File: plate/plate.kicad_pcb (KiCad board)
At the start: 2 copper layers, 67.2 x 29.1 mm, 4 parts

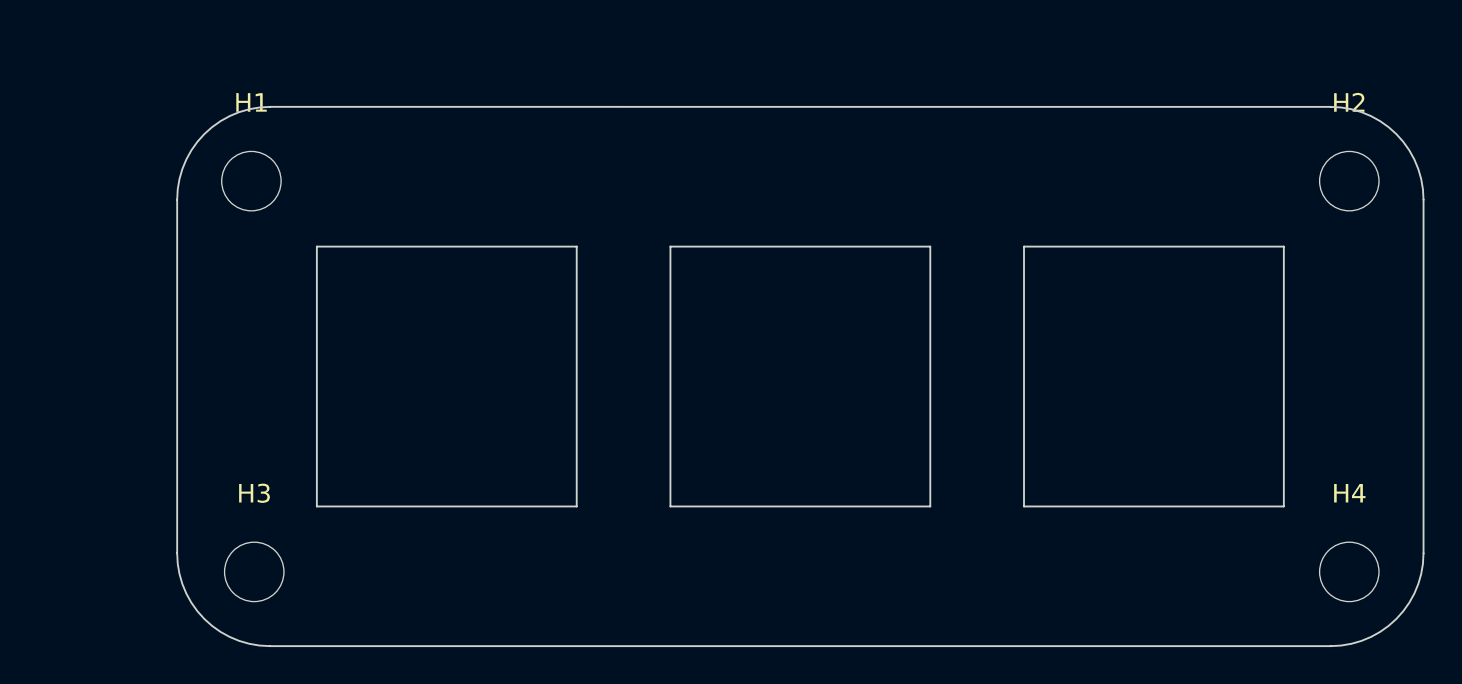
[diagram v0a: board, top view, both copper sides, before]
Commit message: Wire up extra microcontroller pins to a header, align mounting holes
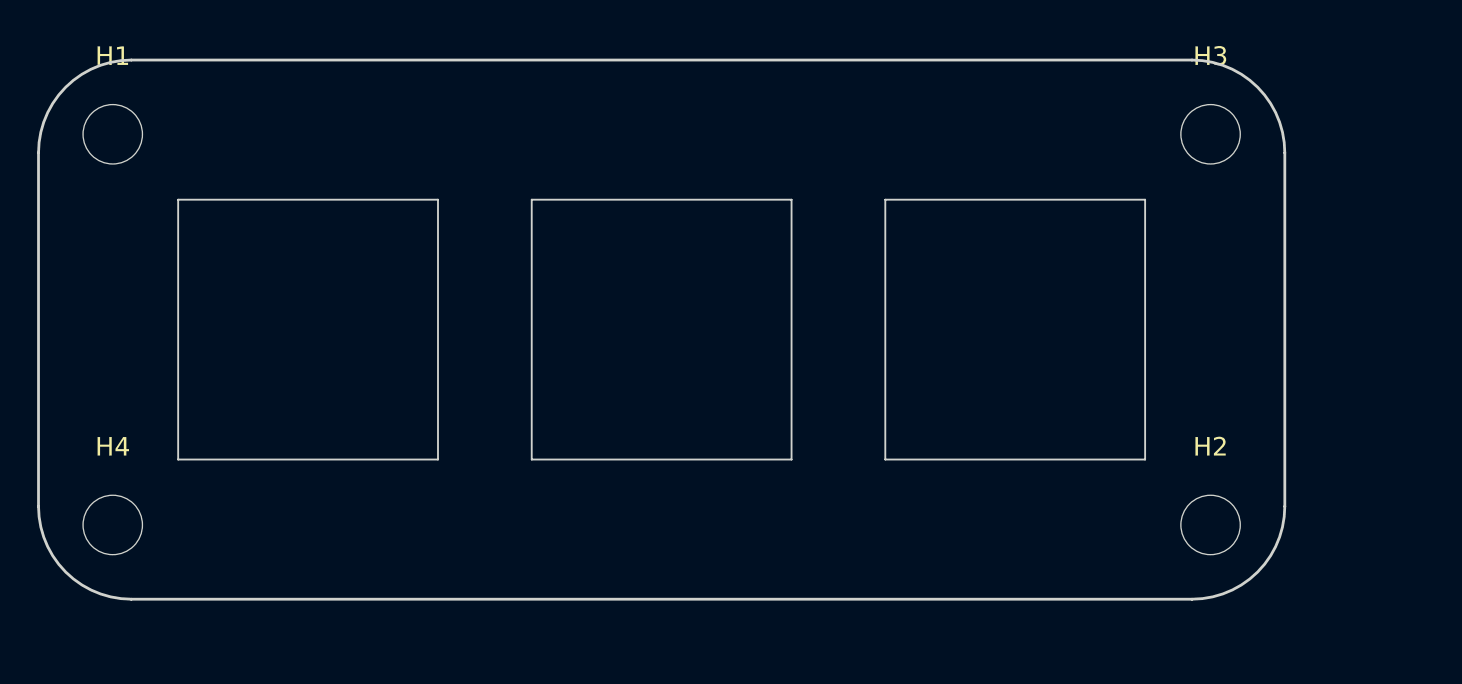
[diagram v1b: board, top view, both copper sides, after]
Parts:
- moved H4 66.7 mm to (114.0, 97.5)
- moved H3 56.7 mm to (173.2, 76.5)
- moved H2 20.0 mm to (173.2, 97.5)
- moved H1 7.89 mm to (114.0, 76.5)
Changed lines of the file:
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@@
     (pad_to_mask_clearance 0)
     (aux_axis_origin 117.496765 74.9968)
-    (grid_origin 122.496765 79.9968)
+    (grid_origin 172.1764 77.4722)
     (pcbplotparams
       (layerselection 0x00010fc_ffffffff)
@@
   (net 0 "")
   (footprint "MountingHole:MountingHole_3.2mm_M3" (layer "F.Cu")
-    (at 180.650815 78.9968)
+    (at 114.026185 97.522207)
+    (descr "Mounting Hole 3.2mm, no annular, M3")
+    (tags "mounting hole 3.2mm no annular m3")
+    (property "Sheetfile" "plate.kicad_sch")
+    (property "Sheetname" "")
+    (attr exclude_from_pos_files)
+    (fp_text reference "H4" (at 0 -4.2) (layer "F.SilkS")
+      (effects (font (size 1 1) (thickness 0.15)))
+    )
+    (fp_text value "MountingHole" (at 0 4.2) (layer "F.Fab")
+      (effects (font (size 1 1) (thickness 0.15)))
+    )
+    (fp_text user "${REFERENCE}" (at 0 0) (layer "F.Fab")
+      (effects (font (size 1 1) (thickness 0.15)))
+    )
+    (fp_circle (center 0 0) (end 3.2 0) (layer "Cmts.User") (width 0.15) (fill none))
+    (fp_circle (center 0 0) (end 3.45 0) (layer "F.CrtYd") (width 0.05) (fill none))
+    (pad "" np_thru_hole circle (at 0 0) (size 3.2 3.2) (drill 3.2) (layers *.Cu *.Mask))
+  )
+  (footprint "MountingHole:MountingHole_3.2mm_M3" (layer "F.Cu")
+    (at 114.0262 76.4722)
+    (descr "Mounting Hole 3.2mm, no annular, M3")
+    (tags "mounting hole 3.2mm no annular m3")
+    (property "Sheetfile" "plate.kicad_sch")
+    (property "Sheetname" "")
+    (attr exclude_from_pos_files)
+    (fp_text reference "H1" (at 0 -4.2) (layer "F.SilkS")
+      (effects (font (size 1 1) (thickness 0.15)))
+    )
+    (fp_text value "MountingHole" (at 0 4.2) (layer "F.Fab")
+      (effects (font (size 1 1) (thickness 0.15)))
+    )
+    (fp_text user "${REFERENCE}" (at 0 0) (layer "F.Fab")
+      (effects (font (size 1 1) (thickness 0.15)))
+    )
+    (fp_circle (center 0 0) (end 3.2 0) (layer "Cmts.User") (width 0.15) (fill none))
+    (fp_circle (center 0 0) (end 3.45 0) (layer "F.CrtYd") (width 0.05) (fill none))
+    (pad "" np_thru_hole circle (at 0 0) (size 3.2 3.2) (drill 3.2) (layers *.Cu *.Mask))
+  )
+  (footprint "MountingHole:MountingHole_3.2mm_M3" (layer "F.Cu")
+    (at 173.1764 97.522207)
     (descr "Mounting Hole 3.2mm, no annular, M3")
     (tags "mounting hole 3.2mm no annular m3")
@@
   )
   (footprint "MountingHole:MountingHole_3.2mm_M3" (layer "F.Cu")
-    (at 180.650815 100.05093)
-    (descr "Mounting Hole 3.2mm, no annular, M3")
-    (tags "mounting hole 3.2mm no annular m3")
-    (property "Sheetfile" "plate.kicad_sch")
-    (property "Sheetname" "")
-    (attr exclude_from_pos_files)
-    (fp_text reference "H4" (at 0 -4.2) (layer "F.SilkS")
-      (effects (font (size 1 1) (thickness 0.15)))
-    )
-    (fp_text value "MountingHole" (at 0 4.2) (layer "F.Fab")
-      (effects (font (size 1 1) (thickness 0.15)))
-    )
-    (fp_text user "${REFERENCE}" (at 0 0) (layer "F.Fab")
-      (effects (font (size 1 1) (thickness 0.15)))
-    )
-    (fp_circle (center 0 0) (end 3.2 0) (layer "Cmts.User") (width 0.15) (fill none))
-    (fp_circle (center 0 0) (end 3.45 0) (layer "F.CrtYd") (width 0.05) (fill none))
-    (pad "" np_thru_hole circle (at 0 0) (size 3.2 3.2) (drill 3.2) (layers *.Cu *.Mask))
-  )
-  (footprint "MountingHole:MountingHole_3.2mm_M3" (layer "F.Cu")
-    (at 121.650815 100.05093)
+    (at 173.1764 76.4722)
     (descr "Mounting Hole 3.2mm, no annular, M3")
     (tags "mounting hole 3.2mm no annular m3")
@@
     (pad "" np_thru_hole circle (at 0 0) (size 3.2 3.2) (drill 3.2) (layers *.Cu *.Mask))
   )
-  (footprint "MountingHole:MountingHole_3.2mm_M3" (layer "F.Cu")
-    (at 121.496765 78.9968)
-    (descr "Mounting Hole 3.2mm, no annular, M3")
-    (tags "mounting hole 3.2mm no annular m3")
-    (property "Sheetfile" "plate.kicad_sch")
-    (property "Sheetname" "")
-    (attr exclude_from_pos_files)
-    (fp_text reference "H1" (at 0 -4.2) (layer "F.SilkS")
-      (effects (font (size 1 1) (thickness 0.15)))
-    )
-    (fp_text value "MountingHole" (at 0 4.2) (layer "F.Fab")
-      (effects (font (size 1 1) (thickness 0.15)))
-    )
-    (fp_text user "${REFERENCE}" (at 0 0) (layer "F.Fab")
-      (effects (font (size 1 1) (thickness 0.15)))
-    )
-    (fp_circle (center 0 0) (end 3.2 0) (layer "Cmts.User") (width 0.15) (fill none))
-    (fp_circle (center 0 0) (end 3.45 0) (layer "F.CrtYd") (width 0.05) (fill none))
-    (pad "" np_thru_hole circle (at 0 0) (size 3.2 3.2) (drill 3.2) (layers *.Cu *.Mask))
-  )
-  (gr_line (start 158.074915 82.5241) (end 158.074915 96.525) (layer "Edge.Cuts") (width 0.1))
-  (gr_line (start 144.074115 96.525) (end 144.074115 82.5241) (layer "Edge.Cuts") (width 0.1))
-  (gr_line (start 179.650815 104.05093) (end 122.496765 104.05093) (layer "Edge.Cuts") (width 0.1))
-  (gr_line (start 144.074115 82.5241) (end 158.074915 82.5241) (layer "Edge.Cuts") (width 0.1))
-  (gr_line (start 125.024105 96.525) (end 125.024105 82.5241) (layer "Edge.Cuts") (width 0.1))
-  (gr_line (start 139.025015 96.525) (end 125.024105 96.525) (layer "Edge.Cuts") (width 0.1))
-  (gr_line (start 177.124915 96.525) (end 163.124215 96.525) (layer "Edge.Cuts") (width 0.1))
-  (gr_arc (start 117.496765 79.9968) (mid 118.961231 76.461266) (end 122.496765 74.9968) (layer "Edge.Cuts") (width 0.1))
-  (gr_line (start 184.650815 79.9968) (end 184.650815 99.05093) (layer "Edge.Cuts") (width 0.1))
-  (gr_line (start 122.496765 74.9936) (end 179.650815 74.9968) (layer "Edge.Cuts") (width 0.1))
-  (gr_arc (start 122.496765 104.05093) (mid 118.961231 102.586464) (end 117.496765 99.05093) (layer "Edge.Cuts") (width 0.1))
-  (gr_arc (start 179.650815 74.9968) (mid 183.186349 76.461266) (end 184.650815 79.9968) (layer "Edge.Cuts") (width 0.1))
-  (gr_line (start 117.496765 99.05093) (end 117.496765 79.9968) (layer "Edge.Cuts") (width 0.1))
-  (gr_line (start 177.124915 82.5241) (end 177.124915 96.525) (layer "Edge.Cuts") (width 0.1))
-  (gr_line (start 163.124215 96.525) (end 163.124215 82.5241) (layer "Edge.Cuts") (width 0.1))
-  (gr_line (start 163.124215 82.5241) (end 177.124915 82.5241) (layer "Edge.Cuts") (width 0.1))
-  (gr_line (start 158.074915 96.525) (end 144.074115 96.525) (layer "Edge.Cuts") (width 0.1))
-  (gr_arc (start 184.650815 99.05093) (mid 183.186349 102.586464) (end 179.650815 104.05093) (layer "Edge.Cuts") (width 0.1))
-  (gr_line (start 125.024105 82.5241) (end 139.025015 82.5241) (layer "Edge.Cuts") (width 0.1))
-  (gr_line (start 139.025015 82.5241) (end 139.025015 96.525) (layer "Edge.Cuts") (width 0.1))
-  (gr_line (start 122.496765 79.9968) (end 179.650815 79.9968) (layer "User.1") (width 0.1))
-  (gr_line (start 179.650815 99.05093) (end 122.496765 99.05093) (layer "User.1") (width 0.1))
-  (gr_line (start 122.496765 99.05093) (end 122.496765 79.9968) (layer "User.1") (width 0.1))
-  (gr_line (start 179.650815 79.9968) (end 179.650815 99.05093) (layer "User.1") (width 0.1))
+  (gr_line (start 172.1764 101.522207) (end 115.026185 101.522207) (layer "Edge.Cuts") (width 0.15))
+  (gr_line (start 150.6001 93.99626) (end 136.6008 93.99626) (layer "Edge.Cuts") (width 0.1))
+  (gr_line (start 169.6501 79.9968) (end 169.6501 93.99626) (layer "Edge.Cuts") (width 0.1))
+  (gr_line (start 110.026185 96.522207) (end 110.026185 77.4722) (layer "Edge.Cuts") (width 0.15))
+  (gr_arc (start 115.026185 101.522207) (mid 111.490651 100.057741) (end 110.026185 96.522207) (layer "Edge.Cuts") (width 0.15))
+  (gr_line (start 150.6001 79.9968) (end 150.6001 93.99626) (layer "Edge.Cuts") (width 0.1))
+  (gr_line (start 155.6508 93.99626) (end 155.6508 79.9968) (layer "Edge.Cuts") (width 0.1))
+  (gr_arc (start 172.1764 72.4722) (mid 175.711934 73.936666) (end 177.1764 77.4722) (layer "Edge.Cuts") (width 0.15))
+  (gr_line (start 131.5503 79.9968) (end 131.5503 93.99626) (layer "Edge.Cuts") (width 0.1))
+  (gr_line (start 155.6508 79.9968) (end 169.6501 79.9968) (layer "Edge.Cuts") (width 0.1))
+  (gr_line (start 177.1764 77.4722) (end 177.1764 96.522207) (layer "Edge.Cuts") (width 0.15))
+  (gr_arc (start 110.026185 77.4722) (mid 111.490651 73.936666) (end 115.026185 72.4722) (layer "Edge.Cuts") (width 0.15))
+  (gr_line (start 117.55075 93.99626) (end 117.55075 79.9968) (layer "Edge.Cuts") (width 0.1))
+  (gr_line (start 136.6008 93.99626) (end 136.6008 79.9968) (layer "Edge.Cuts") (width 0.1))
+  (gr_line (start 136.6008 79.9968) (end 150.6001 79.9968) (layer "Edge.Cuts") (width 0.1))
+  (gr_line (start 131.5503 93.99626) (end 117.55075 93.99626) (layer "Edge.Cuts") (width 0.1))
+  (gr_line (start 169.6501 93.99626) (end 155.6508 93.99626) (layer "Edge.Cuts") (width 0.1))
+  (gr_arc (start 177.1764 96.522207) (mid 175.711934 100.057741) (end 172.1764 101.522207) (layer "Edge.Cuts") (width 0.15))
+  (gr_line (start 115.026185 72.4722) (end 172.1764 72.4722) (layer "Edge.Cuts") (width 0.15))
+  (gr_line (start 117.55075 79.9968) (end 131.5503 79.9968) (layer "Edge.Cuts") (width 0.1))
+  (gr_line (start 115.026185 96.522207) (end 115.026185 77.4722) (layer "User.1") (width 0.1))
+  (gr_line (start 150.6001 79.9968) (end 136.6008 93.99626) (layer "User.1") (width 0.15))
+  (gr_line (start 172.1764 77.4722) (end 172.1764 96.522207) (layer "User.1") (width 0.1))
+  (gr_line (start 136.6008 79.9968) (end 150.6001 93.99626) (layer "User.1") (width 0.15))
+  (gr_line (start 172.1764 96.522207) (end 115.026185 96.522207) (layer "User.1") (width 0.1))
+  (gr_line (start 115.026185 77.4722) (end 172.1764 77.4722) (layer "User.1") (width 0.1))
 )

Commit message: Fix DRC, add order number location
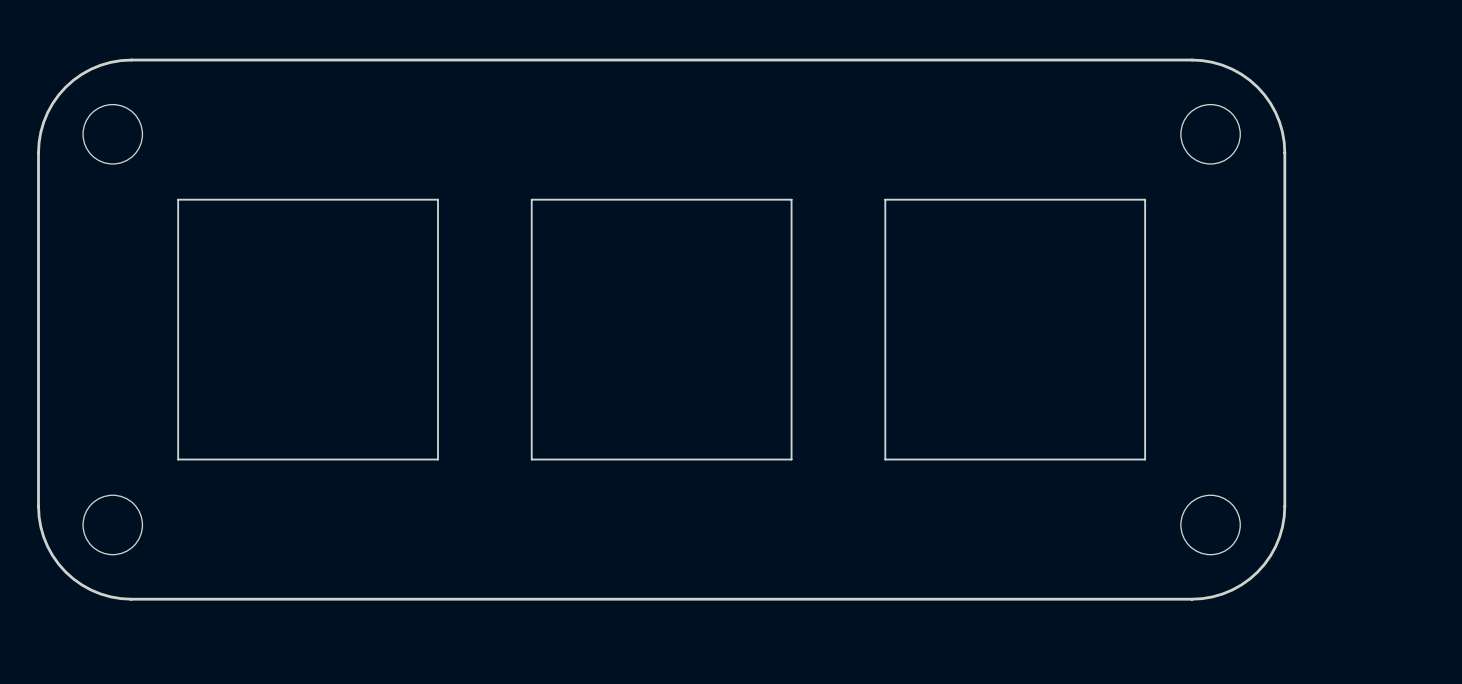
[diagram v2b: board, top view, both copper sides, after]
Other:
- board text added: "JLCJCJLCJLC"
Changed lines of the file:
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@@
     (property "Sheetname" "")
     (attr exclude_from_pos_files)
-    (fp_text reference "H4" (at 0 -4.2) (layer "F.SilkS")
+    (fp_text reference "H4" (at 0 -4.2) (layer "F.SilkS") hide
       (effects (font (size 1 1) (thickness 0.15)))
     )
@@
     (property "Sheetname" "")
     (attr exclude_from_pos_files)
-    (fp_text reference "H1" (at 0 -4.2) (layer "F.SilkS")
+    (fp_text reference "H1" (at 0 -4.2) (layer "F.SilkS") hide
       (effects (font (size 1 1) (thickness 0.15)))
     )
@@
     (property "Sheetname" "")
     (attr exclude_from_pos_files)
-    (fp_text reference "H2" (at 0 -4.2) (layer "F.SilkS")
+    (fp_text reference "H2" (at 0 -4.2) (layer "F.SilkS") hide
       (effects (font (size 1 1) (thickness 0.15)))
     )
@@
     (property "Sheetname" "")
     (attr exclude_from_pos_files)
-    (fp_text reference "H3" (at 0 -4.2) (layer "F.SilkS")
+    (fp_text reference "H3" (at 0 -4.2) (layer "F.SilkS") hide
       (effects (font (size 1 1) (thickness 0.15)))
     )
@@
   (gr_line (start 172.1764 96.522207) (end 115.026185 96.522207) (layer "User.1") (width 0.1))
   (gr_line (start 115.026185 77.4722) (end 172.1764 77.4722) (layer "User.1") (width 0.1))
+  (gr_text "JLCJCJLCJLC" (at 143.6764 78.7222) (layer "B.SilkS")
+    (effects (font (size 1 1) (thickness 0.15)) (justify mirror))
+  )
 )
